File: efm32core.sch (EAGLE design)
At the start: 14 parts

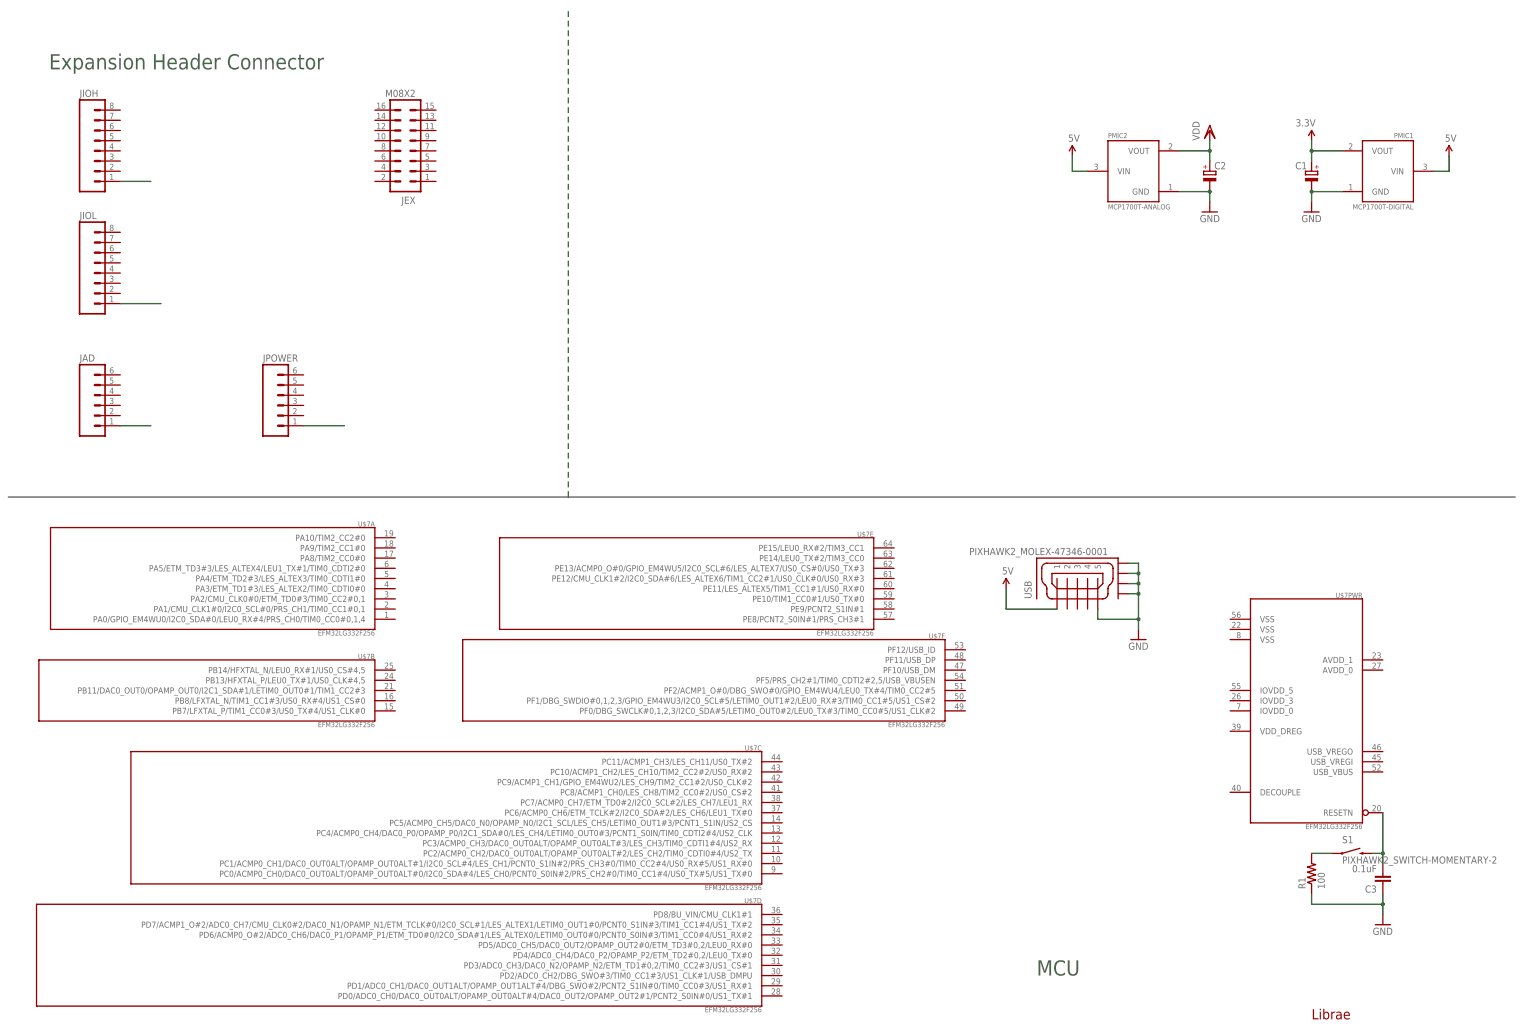
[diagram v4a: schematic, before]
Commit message: modulize, update power and usb
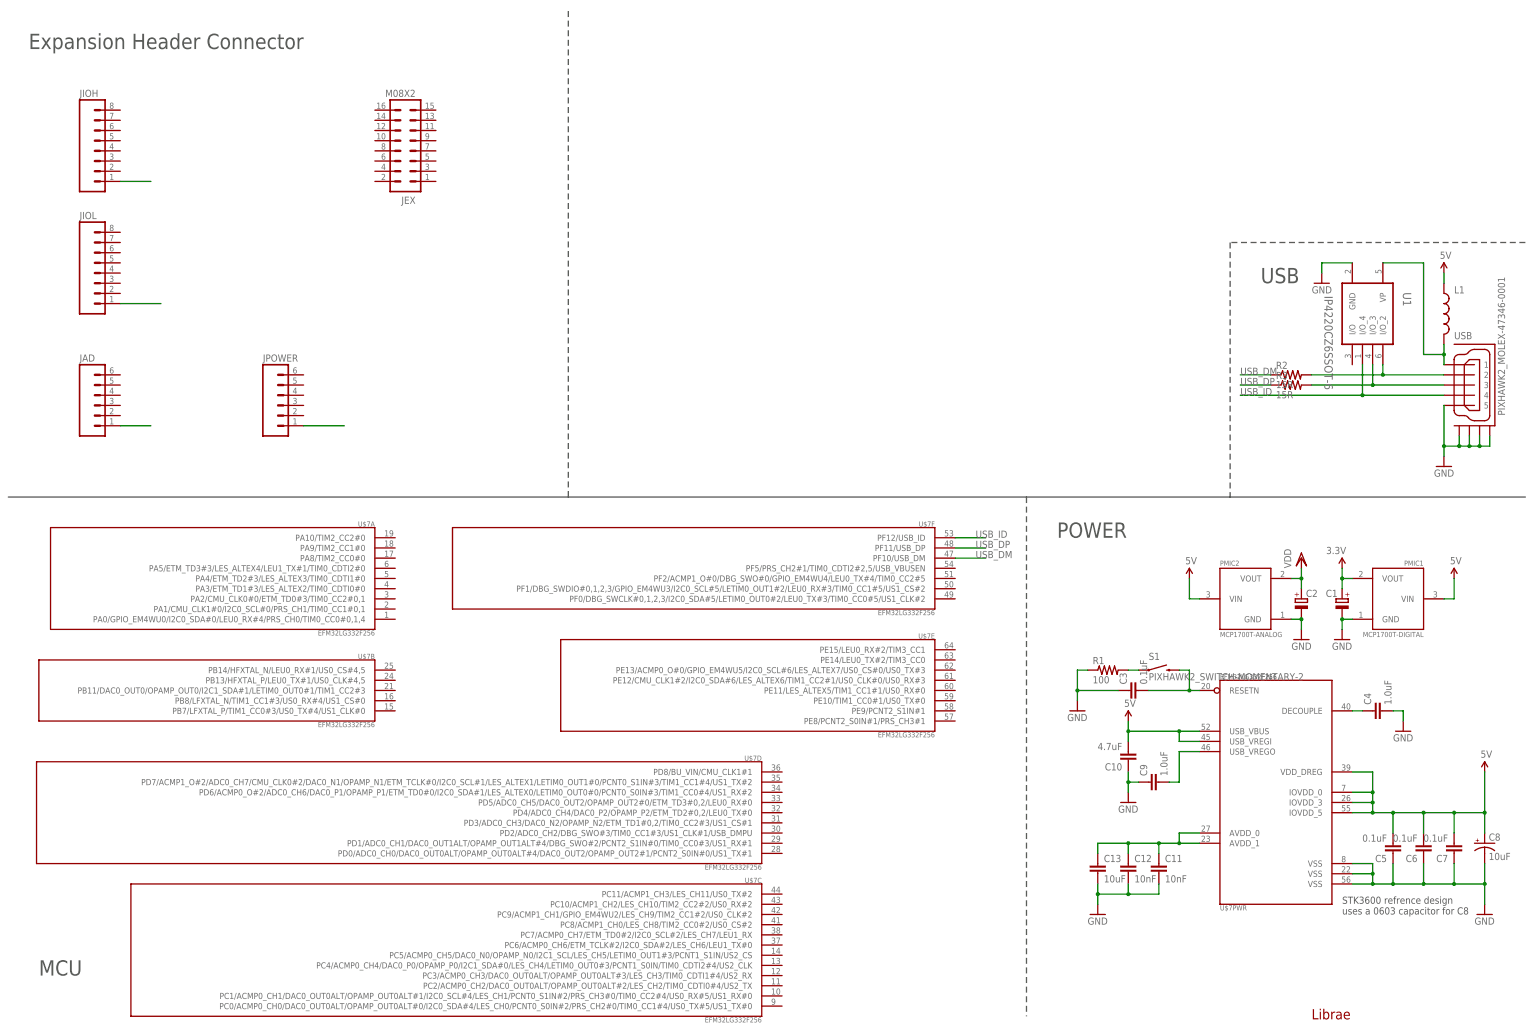
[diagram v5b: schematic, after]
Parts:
- added C10: 4.7uF, SparkFun-Capacitors:4.7UF-6.3V-10%(0603)0603
- added C11, C12: 10nF, SparkFun-Capacitors:10NF/10000PF-50V-10%(0603)
- added C13: 10uF, SparkFun-Capacitors:10UF-6.3V-20%(0603)
- added C4, C9: 1.0uF, SparkFun-Capacitors:1.0UF-16V-10%(0603)
- added C5, C6, C7: 0.1uF, SparkFun-Capacitors:0.1UF-25V-5%(0603)
- added C8: 10uF, SparkFun-Capacitors:10UF-16V-10%(TANT)
- added L1: (no value), SparkFun-Passives:INDUCTOR0603
- added R2, R3: 15R, SparkFun-Resistors:100-1%
- added U1: IP4220CZ6SSOT-6, FT232H-basic:IP4220CZ6SSOT-6
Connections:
- new net 1: L1.2, U1.VP, USB.1
- new net N$10: C11.1, C12.1, C13.1, U$7PWR.AVDD_0, U$7PWR.AVDD_1
- new net N$13: R3.2, U1.I/O_3, USB.3
- new net N$14: R2.2, U1.I/O_2, USB.2
- new net N$7: C4.1, U$7PWR.DECOUPLE
- new net N$8: C9.2, U$7PWR.USB_VREGO
- new net USB_DM: R2.1, U$7F.PF10/USB_DM
- new net USB_DP: R3.1, U$7F.PF11/USB_DP
- new net USB_ID: U$7F.PF12/USB_ID, U1.I/O_4, USB.4
- net 5V: now also C10.2, C5.2, C6.2, C7.2, C8.+, L1.1, U$7PWR.IOVDD_0, U$7PWR.IOVDD_3, U$7PWR.IOVDD_5, U$7PWR.USB_VBUS, U$7PWR.USB_VREGI, U$7PWR.VDD_DREG; no longer USB.1
- net GND: now also C10.1, C11.2, C12.2, C13.2, C4.2, C5.1, C6.1, C7.1, C8.-, C9.1, U$7PWR.VSS@1, U$7PWR.VSS@2, U$7PWR.VSS@3, U1.GND, USB.GND4
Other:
- note added: "POWER"
- note added: "STK3600 refrence design uses a 0603 capacitor for C8"
- note added: "USB"
- moved on the sheet: C1, C2, C3, PMIC1, PMIC2, R1, S1, U$7C, U$7D, U$7E, U$7F, U$7PWR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

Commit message: optimize a bit
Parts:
- added C14: 1uF, SparkFun-Capacitors:10UF-6.3V-20%(1206)
- added STANDOFF1, STANDOFF2, STANDOFF3, STANDOFF4: STAND-OFF, SparkFun-Electromechanical:STAND-OFF
- C1, C2: value (none) -> 1uF; device maple-r5:CPOL-EUUD-4X5,8 -> SparkFun-Capacitors:10UF-6.3V-20%(1206)
- C13: device SparkFun-Capacitors:10UF-6.3V-20%(0603) -> SparkFun-Capacitors:10UF-6.3V-20%(1206)
- C8: device SparkFun-Capacitors:10UF-16V-10%(TANT) -> SparkFun-Capacitors:10UF-6.3V-20%(1206)
- renumbered U$7 to MCU
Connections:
- removed net N$4: JPOWER.1
- removed net N$5: C3.2, MCUPWR.RESETN, S1.2
- new net ADCH0: MCUD.PD0/ADC0_CH0/DAC0_OUT0ALT/OPAMP_OUT0ALT#4/DAC0_OUT2/OPAMP_OUT2#1/PCNT2_S0IN#0/US1_TX#1
- new net ADCH1: MCUD.PD1/ADC0_CH1/DAC0_OUT1ALT/OPAMP_OUT1ALT#4/DBG_SWO#2/PCNT2_S1IN#0/TIM0_CC0#3/US1_RX#1
- new net ADCH2: MCUD.PD2/ADC0_CH2/DBG_SWO#3/TIM0_CC1#3/US1_CLK#1/USB_DMPU
- new net ADCH3: MCUD.PD3/ADC0_CH3/DAC0_N2/OPAMP_N2/ETM_TD1#0,2/TIM0_CC2#3/US1_CS#1
- new net ADCH4: MCUD.PD4/ADC0_CH4/DAC0_P2/OPAMP_P2/ETM_TD2#0,2/LEU0_TX#0
- new net ADCH5: MCUD.PD5/ADC0_CH5/DAC0_OUT2/OPAMP_OUT2#0/ETM_TD3#0,2/LEU0_RX#0
- new net PD6: MCUD.PD6/ACMP0_O#2/ADC0_CH6/DAC0_P1/OPAMP_P1/ETM_TD0#0/I2C0_SDA#1/LES_ALTEX0/LETIM0_OUT0#0/PCNT0_S0IN#3/TIM1_CC0#4/US1_RX#2
- new net PD7: MCUD.PD7/ACMP1_O#2/ADC0_CH7/CMU_CLK0#2/DAC0_N1/OPAMP_N1/ETM_TCLK#0/I2C0_SCL#1/LES_ALTEX1/LETIM0_OUT1#0/PCNT0_S1IN#3/TIM1_CC1#4/US1_TX#2
- new net PD8: MCUD.PD8/BU_VIN/CMU_CLK1#1
- new net RESET: C3.2, JPOWER.1, MCUPWR.RESETN, S1.2
- new net VIN: JPOWER.6
- net 3.3V: now also C1.1, JPOWER.2; no longer C1.+
- net 5V: now also C14.1, C8.2; no longer C8.+
- net GND: now also C1.2, C14.2, C2.2, C8.1, JPOWER.4, JPOWER.5; no longer C1.-, C2.-, C8.-
- net VDD: now also C2.1, JPOWER.3; no longer C2.+

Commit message: update a bit
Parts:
- added R4, R5: 100, SparkFun-Resistors:100OHM1/10W1%(0603)
- added S2: PIXHAWK2_SWITCH-MOMENTARY-2, PX4FMUv1.7.1:PIXHAWK2_SWITCH-MOMENTARY-2
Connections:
- new net N$5: R4.1
- net 3.3V: now also R5.2
- net ADCH0: now also JAD.1
- net ADCH1: now also JAD.2
- net ADCH2: now also JAD.3
- net ADCH3: now also JAD.4
- net ADCH4: now also JAD.5
- net ADCH5: now also JAD.6
- net N$2: now also R4.2, S2.1; no longer JAD.1
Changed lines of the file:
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@@
 <grid distance="0.1" unitdist="inch" unit="inch" style="lines" multiple="1" display="yes" altdistance="0.01" altunitdist="inch" altunit="inch"/>
 <layers>
-<layer number="1" name="Top" color="4" fill="1" visible="yes" active="no"/>
-<layer number="16" name="Bottom" color="1" fill="1" visible="yes" active="no"/>
-<layer number="17" name="Pads" color="2" fill="1" visible="yes" active="no"/>
-<layer number="18" name="Vias" color="2" fill="1" visible="yes" active="no"/>
-<layer number="19" name="Unrouted" color="6" fill="1" visible="yes" active="no"/>
-<layer number="20" name="Dimension" color="15" fill="1" visible="yes" active="no"/>
-<layer number="21" name="tPlace" color="7" fill="1" visible="yes" active="no"/>
-<layer number="22" name="bPlace" color="7" fill="1" visible="yes" active="no"/>
-<layer number="23" name="tOrigins" color="15" fill="1" visible="yes" active="no"/>
-<layer number="24" name="bOrigins" color="15" fill="1" visible="yes" active="no"/>
-<layer number="25" name="tNames" color="7" fill="1" visible="yes" active="no"/>
-<layer number="26" name="bNames" color="7" fill="1" visible="yes" active="no"/>
-<layer number="27" name="tValues" color="7" fill="1" visible="yes" active="no"/>
-<layer number="28" name="bValues" color="7" fill="1" visible="yes" active="no"/>
+<layer number="1" name="Top" color="4" fill="1" visible="no" active="no"/>
+<layer number="16" name="Bottom" color="1" fill="1" visible="no" active="no"/>
+<layer number="17" name="Pads" color="2" fill="1" visible="no" active="no"/>
+<layer number="18" name="Vias" color="2" fill="1" visible="no" active="no"/>
+<layer number="19" name="Unrouted" color="6" fill="1" visible="no" active="no"/>
+<layer number="20" name="Dimension" color="15" fill="1" visible="no" active="no"/>
+<layer number="21" name="tPlace" color="7" fill="1" visible="no" active="no"/>
+<layer number="22" name="bPlace" color="7" fill="1" visible="no" active="no"/>
+<layer number="23" name="tOrigins" color="15" fill="1" visible="no" active="no"/>
+<layer number="24" name="bOrigins" color="15" fill="1" visible="no" active="no"/>
+<layer number="25" name="tNames" color="7" fill="1" visible="no" active="no"/>
+<layer number="26" name="bNames" color="7" fill="1" visible="no" active="no"/>
+<layer number="27" name="tValues" color="7" fill="1" visible="no" active="no"/>
+<layer number="28" name="bValues" color="7" fill="1" visible="no" active="no"/>
 <layer number="29" name="tStop" color="7" fill="3" visible="no" active="no"/>
 <layer number="30" name="bStop" color="7" fill="6" visible="no" active="no"/>
@@
 <layer number="35" name="tGlue" color="7" fill="4" visible="no" active="no"/>
 <layer number="36" name="bGlue" color="7" fill="5" visible="no" active="no"/>
-<layer number="37" name="tTest" color="7" fill="1" visible="yes" active="no"/>
-<layer number="38" name="bTest" color="7" fill="1" visible="yes" active="no"/>
+<layer number="37" name="tTest" color="7" fill="1" visible="no" active="no"/>
+<layer number="38" name="bTest" color="7" fill="1" visible="no" active="no"/>
 <layer number="39" name="tKeepout" color="4" fill="11" visible="no" active="no"/>
 <layer number="40" name="bKeepout" color="1" fill="11" visible="no" active="no"/>
@@
 <layer number="44" name="Drills" color="7" fill="1" visible="no" active="no"/>
 <layer number="45" name="Holes" color="7" fill="1" visible="no" active="no"/>
-<layer number="46" name="Milling" color="3" fill="1" visible="yes" active="no"/>
-<layer number="47" name="Measures" color="7" fill="1" visible="yes" active="no"/>
-<layer number="48" name="Document" color="7" fill="1" visible="yes" active="no"/>
-<layer number="49" name="Reference" color="7" fill="1" visible="yes" active="no"/>
-<layer number="50" name="dxf" color="7" fill="1" visible="yes" active="no"/>
-<layer number="51" name="tDocu" color="14" fill="1" visible="yes" active="no"/>
-<layer number="52" name="bDocu" color="6" fill="1" visible="yes" active="no"/>
-<layer number="53" name="tGND_GNDA" color="7" fill="9" visible="yes" active="no"/>
-<layer number="54" name="bGND_GNDA" color="1" fill="9" visible="yes" active="no"/>
-<layer number="56" name="wert" color="7" fill="1" visible="yes" active="no"/>
-<layer number="57" name="tCAD" color="7" fill="1" visible="yes" active="no"/>
-<layer number="58" name="bCAD" color="7" fill="1" visible="yes" active="no"/>
+<layer number="46" name="Milling" color="3" fill="1" visible="no" active="no"/>
+<layer number="47" name="Measures" color="7" fill="1" visible="no" active="no"/>
+<layer number="48" name="Document" color="7" fill="1" visible="no" active="no"/>
+<layer number="49" name="Reference" color="7" fill="1" visible="no" active="no"/>
+<layer number="50" name="dxf" color="7" fill="1" visible="no" active="no"/>
+<layer number="51" name="tDocu" color="14" fill="1" visible="no" active="no"/>
+<layer number="52" name="bDocu" color="6" fill="1" visible="no" active="no"/>
+<layer number="53" name="tGND_GNDA" color="7" fill="9" visible="no" active="no"/>
+<layer number="54" name="bGND_GNDA" color="1" fill="9" visible="no" active="no"/>
+<layer number="56" name="wert" color="7" fill="1" visible="no" active="no"/>
+<layer number="57" name="tCAD" color="7" fill="1" visible="no" active="no"/>
+<layer number="58" name="bCAD" color="7" fill="1" visible="no" active="no"/>
 <layer number="91" name="Nets" color="2" fill="1" visible="yes" active="yes"/>
 <layer number="92" name="Busses" color="1" fill="1" visible="yes" active="yes"/>
@@
 <part name="STANDOFF1" library="SparkFun-Electromechanical" deviceset="STAND-OFF" device=""/>
 <part name="STANDOFF2" library="SparkFun-Electromechanical" deviceset="STAND-OFF" device=""/>
+<part name="STANDOFF4" library="SparkFun-Electromechanical" deviceset="STAND-OFF" device=""/>
 <part name="STANDOFF3" library="SparkFun-Electromechanical" deviceset="STAND-OFF" device=""/>
-<part name="STANDOFF4" library="SparkFun-Electromechanical" deviceset="STAND-OFF" device=""/>
+<part name="S2" library="PX4FMUv1.7.1" deviceset="PIXHAWK2_SWITCH-MOMENTARY-2" device=""/>
+<part name="R4" library="SparkFun-Resistors" deviceset="100OHM1/10W1%(0603)" device="" value="100"/>
+<part name="R5" library="SparkFun-Resistors" deviceset="100OHM1/10W1%(0603)" device="" value="100"/>
+<part name="3.3V1" library="SparkFun-Aesthetics" deviceset="3.3V" device=""/>
 </parts>
 <sheets>
@@
 <instance part="STANDOFF1" gate="G$1" x="114.3" y="248.92"/>
 <instance part="STANDOFF2" gate="G$1" x="119.38" y="248.92"/>
+<instance part="STANDOFF4" gate="G$1" x="129.54" y="248.92"/>
 <instance part="STANDOFF3" gate="G$1" x="124.46" y="248.92"/>
-<instance part="STANDOFF4" gate="G$1" x="129.54" y="248.92"/>
+<instance part="S2" gate="G$1" x="233.68" y="38.1"/>
+<instance part="R4" gate="G$1" x="220.98" y="38.1"/>
+<instance part="R5" gate="G$1" x="246.38" y="38.1"/>
+<instance part="3.3V1" gate="G$1" x="254" y="43.18" rot="MR0"/>
 </instances>
 <busses>
@@
 <pinref part="JIOH" gate="G$1" pin="1"/>
 <wire x1="33.02" y1="213.36" x2="40.64" y2="213.36" width="0.1524" layer="91"/>
-</segment>
-</net>
-<net name="N$2" class="0">
-<segment>
-<pinref part="JAD" gate="G$1" pin="1"/>
-<wire x1="33.02" y1="152.4" x2="40.64" y2="152.4" width="0.1524" layer="91"/>
 </segment>
 </net>
@@
 <wire x1="78.74" y1="154.94" x2="86.36" y2="154.94" width="0.1524" layer="91"/>
 <label x="83.82" y="154.94" size="1.778" layer="95"/>
+</segment>
+<segment>
+<pinref part="R5" gate="G$1" pin="2"/>
+<wire x1="251.46" y1="38.1" x2="254" y2="38.1" width="0.1524" layer="91"/>
+<wire x1="254" y1="38.1" x2="254" y2="43.18" width="0.1524" layer="91"/>
+<pinref part="3.3V1" gate="G$1" pin="3.3V"/>
 </segment>
 </net>
@@
 <label x="203.2" y="45.72" size="1.778" layer="95"/>
 </segment>
+<segment>
+<pinref part="JAD" gate="G$1" pin="1"/>
+<wire x1="33.02" y1="152.4" x2="40.64" y2="152.4" width="0.1524" layer="91"/>
+<label x="35.56" y="152.4" size="1.778" layer="95"/>
+</segment>
 </net>
 <net name="ADCH1" class="0">
@@
 <label x="203.2" y="48.26" size="1.778" layer="95"/>
 </segment>
+<segment>
+<pinref part="JAD" gate="G$1" pin="2"/>
+<wire x1="33.02" y1="154.94" x2="40.64" y2="154.94" width="0.1524" layer="91"/>
+<label x="35.56" y="154.94" size="1.778" layer="95"/>
+</segment>
 </net>
 <net name="ADCH2" class="0">
@@
 <label x="203.2" y="50.8" size="1.778" layer="95"/>
 </segment>
+<segment>
+<pinref part="JAD" gate="G$1" pin="3"/>
+<wire x1="33.02" y1="157.48" x2="40.64" y2="157.48" width="0.1524" layer="91"/>
+<label x="35.56" y="157.48" size="1.778" layer="95"/>
+</segment>
 </net>
 <net name="ADCH3" class="0">
@@
 <label x="203.2" y="53.34" size="1.778" layer="95"/>
 </segment>
+<segment>
+<pinref part="JAD" gate="G$1" pin="4"/>
+<wire x1="33.02" y1="160.02" x2="40.64" y2="160.02" width="0.1524" layer="91"/>
+<label x="35.56" y="160.02" size="1.778" layer="95"/>
+</segment>
 </net>
 <net name="ADCH4" class="0">
@@
 <label x="203.2" y="55.88" size="1.778" layer="95"/>
 </segment>
+<segment>
+<pinref part="JAD" gate="G$1" pin="5"/>
+<wire x1="33.02" y1="162.56" x2="40.64" y2="162.56" width="0.1524" layer="91"/>
+<label x="35.56" y="162.56" size="1.778" layer="95"/>
+</segment>
 </net>
 <net name="ADCH5" class="0">
@@
 <label x="203.2" y="58.42" size="1.778" layer="95"/>
 </segment>
+<segment>
+<pinref part="JAD" gate="G$1" pin="6"/>
+<wire x1="33.02" y1="165.1" x2="40.64" y2="165.1" width="0.1524" layer="91"/>
+<label x="35.56" y="165.1" size="1.778" layer="95"/>
+</segment>
 </net>
 <net name="PD6" class="0">
@@
 </segment>
 </net>
+<net name="N$2" class="0">
+<segment>
+<pinref part="R4" gate="G$1" pin="2"/>
+<pinref part="S2" gate="G$1" pin="1"/>
+<wire x1="226.06" y1="38.1" x2="228.6" y2="38.1" width="0.1524" layer="91"/>
+</segment>
+</net>
+<net name="N$5" class="0">
+<segment>
+<pinref part="R4" gate="G$1" pin="1"/>
+<wire x1="215.9" y1="38.1" x2="213.36" y2="38.1" width="0.1524" layer="91"/>
+</segment>
+</net>

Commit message: layout components
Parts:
- added C15, C16: 7p5, SparkFun-Capacitors:9.0PF-50V-10%(0603)
- added C17, C18: 18p, SparkFun-Capacitors:9.0PF-50V-10%(0603)
- added L2: (no value), SparkFun-Passives:INDUCTOR0603
- added R6: 100, SparkFun-Resistors:100OHM1/10W1%(0603)
- added X1: 48.0MHz, adafruit:XTALNX5032
- added X2: 32.768kHz, adafruit:XTALNX5032
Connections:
- removed net N$10: C11.1, C12.1, C13.1, MCUPWR.AVDD_0, MCUPWR.AVDD_1
- new net HFXTAL_N: C15.1, MCUB.PB14/HFXTAL_N/LEU0_RX#1/US0_CS#4,5, X1.P$2
- new net HFXTAL_P: C16.1, MCUB.PB13/HFXTAL_P/LEU0_TX#1/US0_CLK#4,5, X1.P$1
- new net LFXTAL_N: C18.1, MCUB.PB8/LFXTAL_N/TIM1_CC1#3/US0_RX#4/US1_CS#0, X2.P$1
- new net LFXTAL_P: C17.1, MCUB.PB7/LFXTAL_P/TIM1_CC0#3/US0_TX#4/US1_CLK#0, X2.P$2
- new net N$4: L2.2, R6.1
- new net N$9: R5.1, S2.2
- new net PA0: MCUA.PA0/GPIO_EM4WU0/I2C0_SDA#0/LEU0_RX#4/PRS_CH0/TIM0_CC0#0,1,4
- net 3.3V: now also C5.2, C6.2, C7.2, C8.2, L2.1, MCUPWR.IOVDD_0, MCUPWR.IOVDD_3, MCUPWR.IOVDD_5, MCUPWR.VDD_DREG
- net 5V: no longer C5.2, C6.2, C7.2, C8.2, MCUPWR.IOVDD_0, MCUPWR.IOVDD_3, MCUPWR.IOVDD_5, MCUPWR.VDD_DREG
- net GND: now also C15.2, C16.2, C17.2, C18.2
- net VDD: now also C11.1, C12.1, C13.1, MCUPWR.AVDD_0, MCUPWR.AVDD_1, R6.2
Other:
- note added: "CLOCK"
- note added: "add only when lack of power"
- moved on the sheet: C11, C12, C13, R4, R5, S2
